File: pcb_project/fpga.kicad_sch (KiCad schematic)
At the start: 33 parts, among them U1 XC7A100T-FTG256

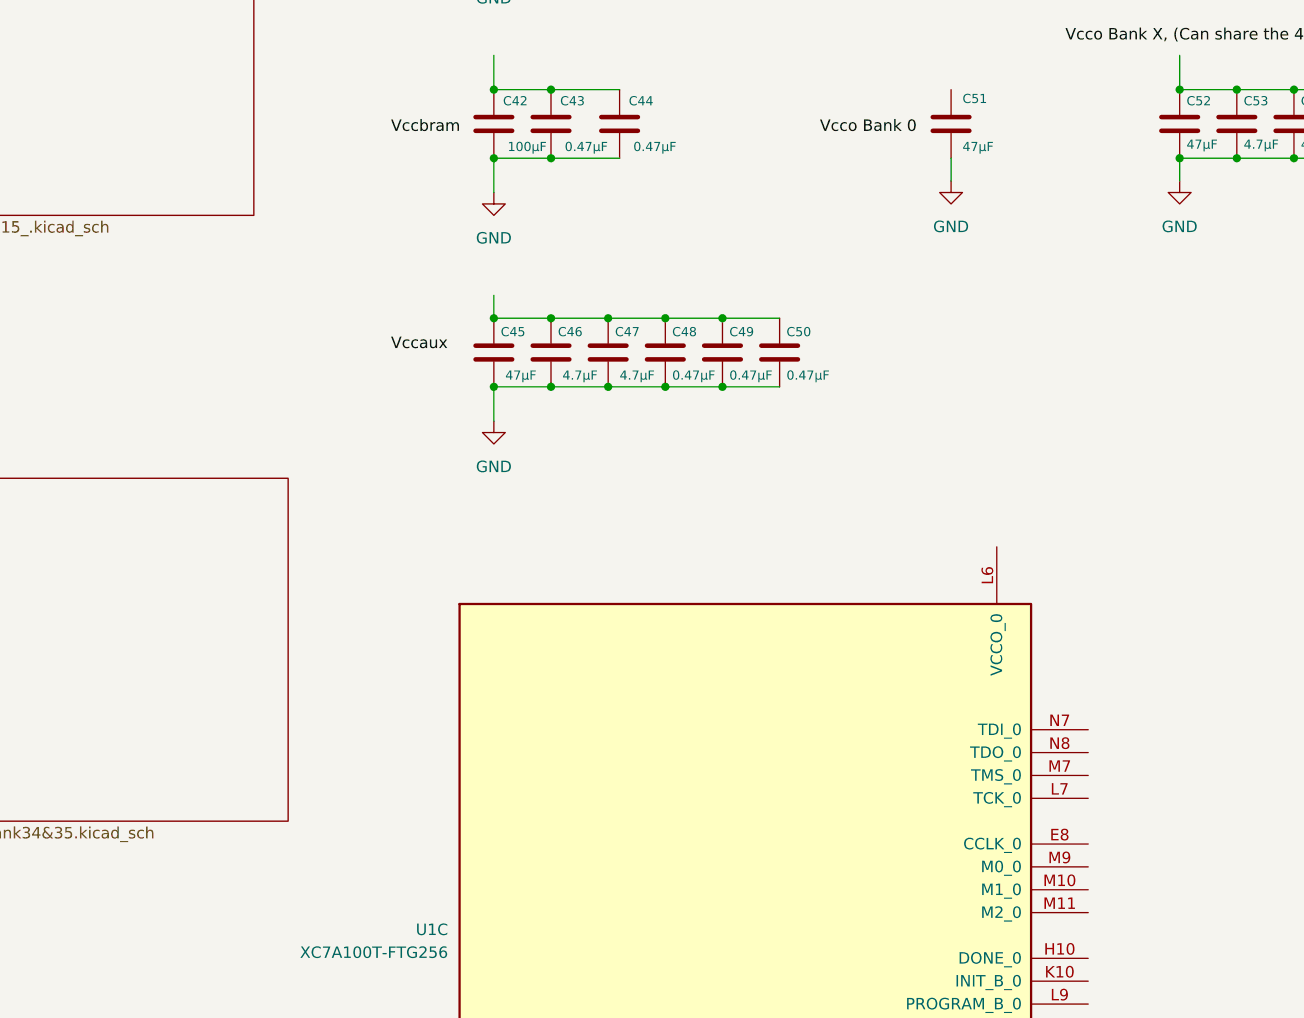
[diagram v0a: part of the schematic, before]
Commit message: Crystal + SPI flash FPGA
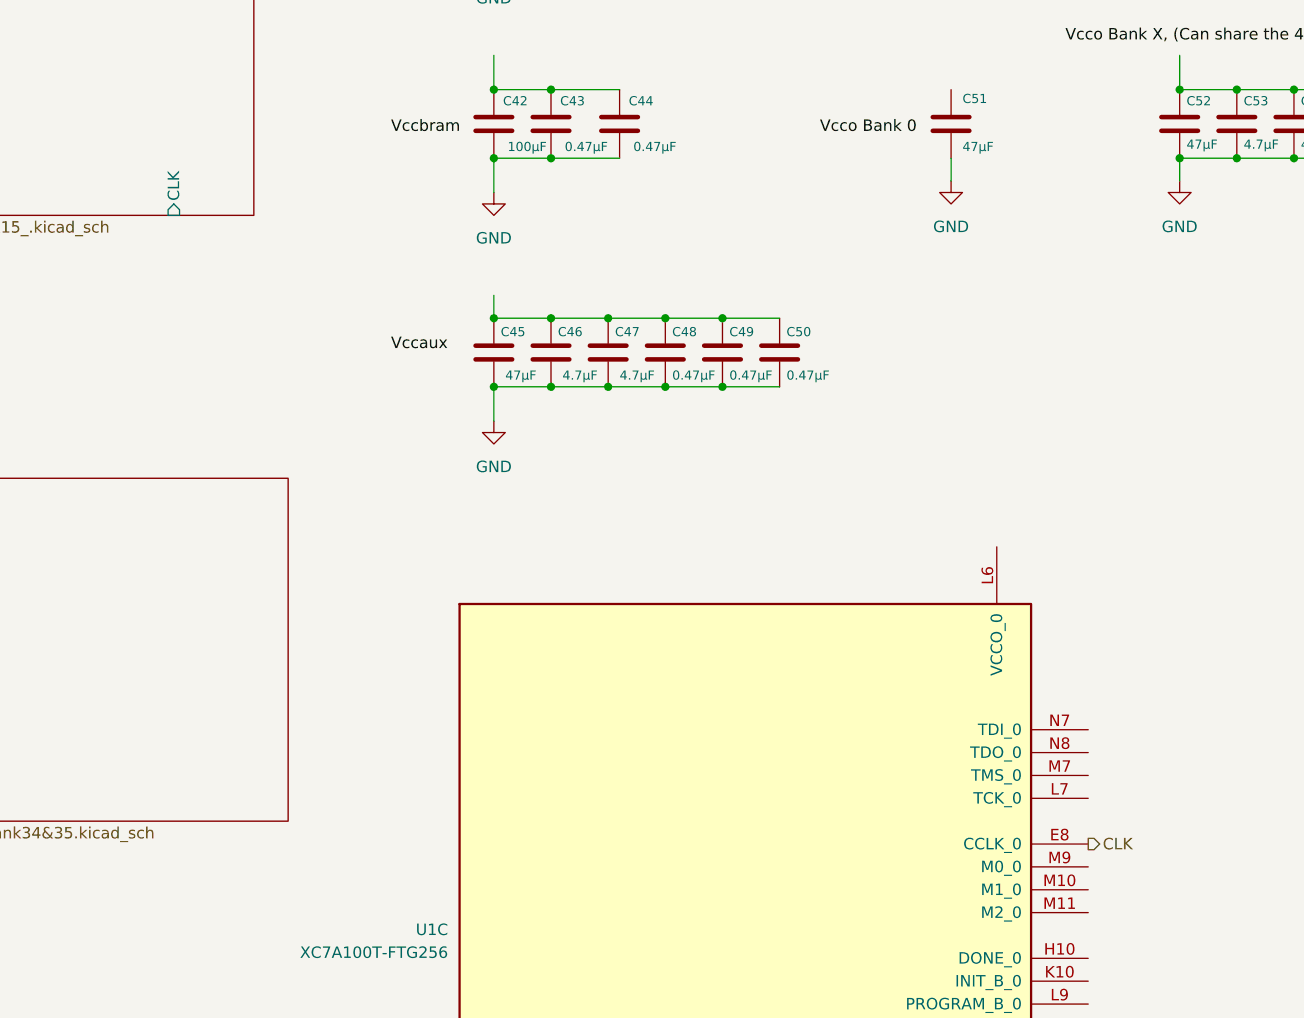
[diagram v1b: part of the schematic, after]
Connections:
- net CLK: now reaches U1.E8 (CCLK_0)
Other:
- sheet A_Bank14&15 ports: added CLK; removed none
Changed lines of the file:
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@@
 		)
 	)
+	(hierarchical_label "CLK"
+		(shape output)
+		(at 167.64 134.62 0)
+		(effects
+			(font
+				(size 1.27 1.27)
+			)
+			(justify left)
+		)
+	)
 	(symbol
 		(lib_id "Device:C")
@@
 			)
 		)
+		(pin "CLK" input
+			(at 66.04 64.77 270)
+			(effects
+				(font
+					(size 1.27 1.27)
+				)
+				(justify left)
+			)
+		)

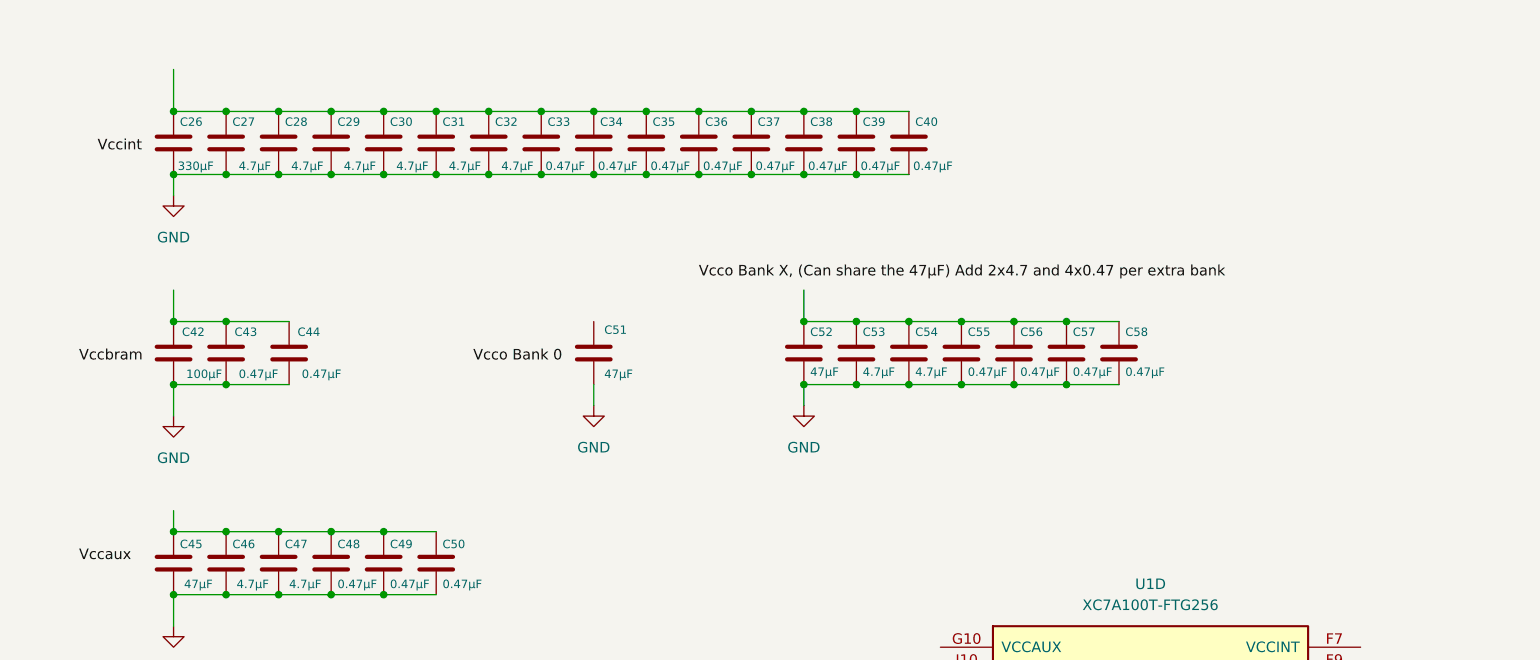
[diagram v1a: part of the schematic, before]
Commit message: Add framebuffer SRAM
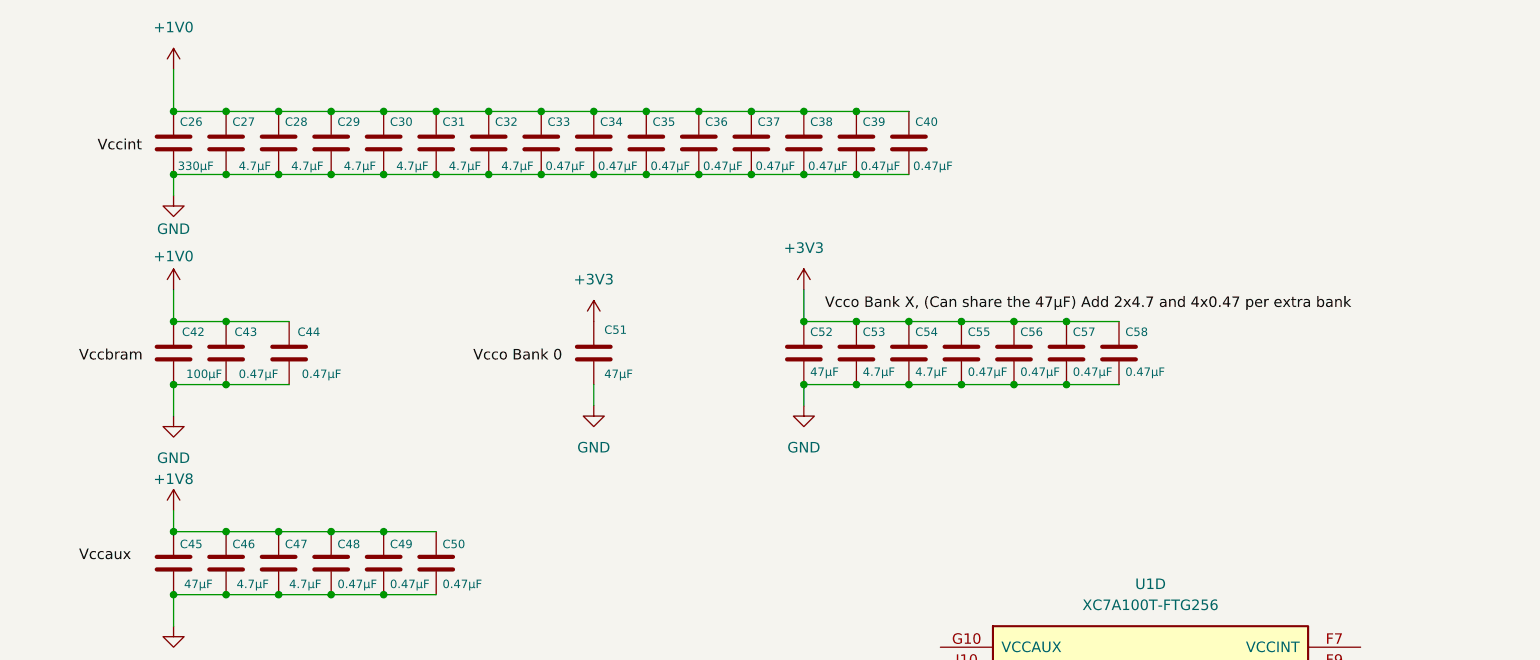
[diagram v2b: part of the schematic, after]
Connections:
- net +1V8: now reaches C45.1, C46.1, C47.1, C48.1, C49.1, C50.1
- net +3V3: now reaches C52.1, C53.1, C54.1, C55.1, C56.1, C57.1, C58.1
- net +3V3: now also C51.1
- net +1V0: now reaches C26.1, C27.1, C28.1, C29.1, C30.1, C31.1, C32.1, C33.1, C34.1, C35.1, C36.1, C37.1, C38.1, C39.1, C40.1
- net +1V0: now also C42.1, C43.1, C44.1

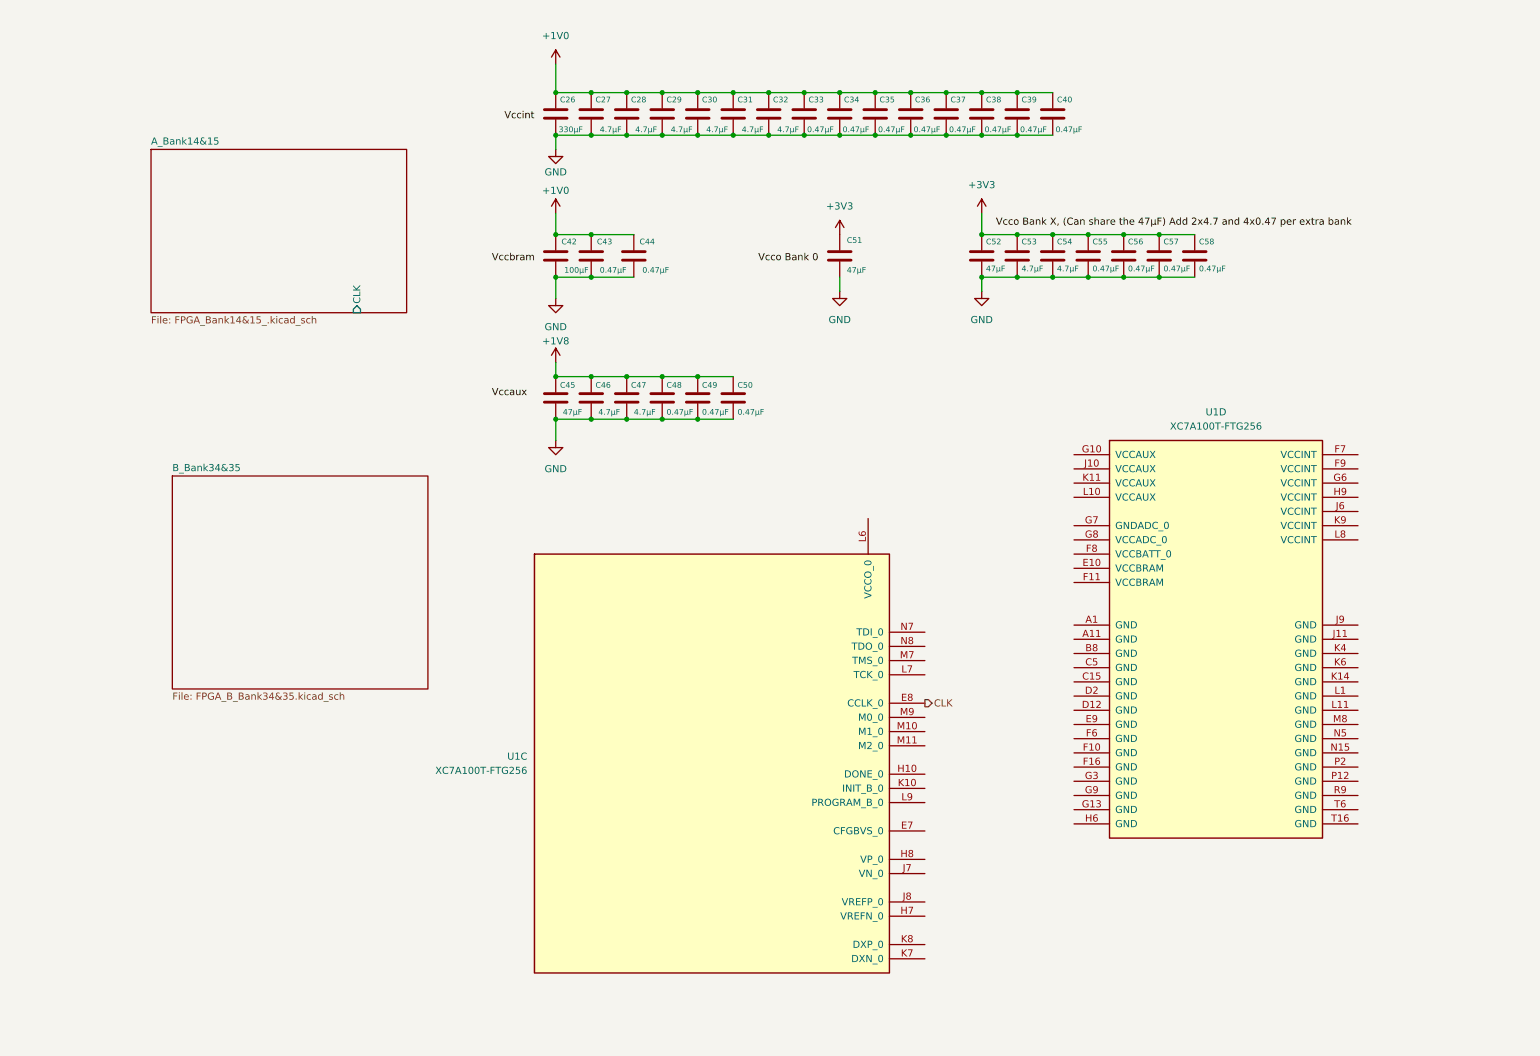
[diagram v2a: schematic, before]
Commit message: Add FPGA JTAG
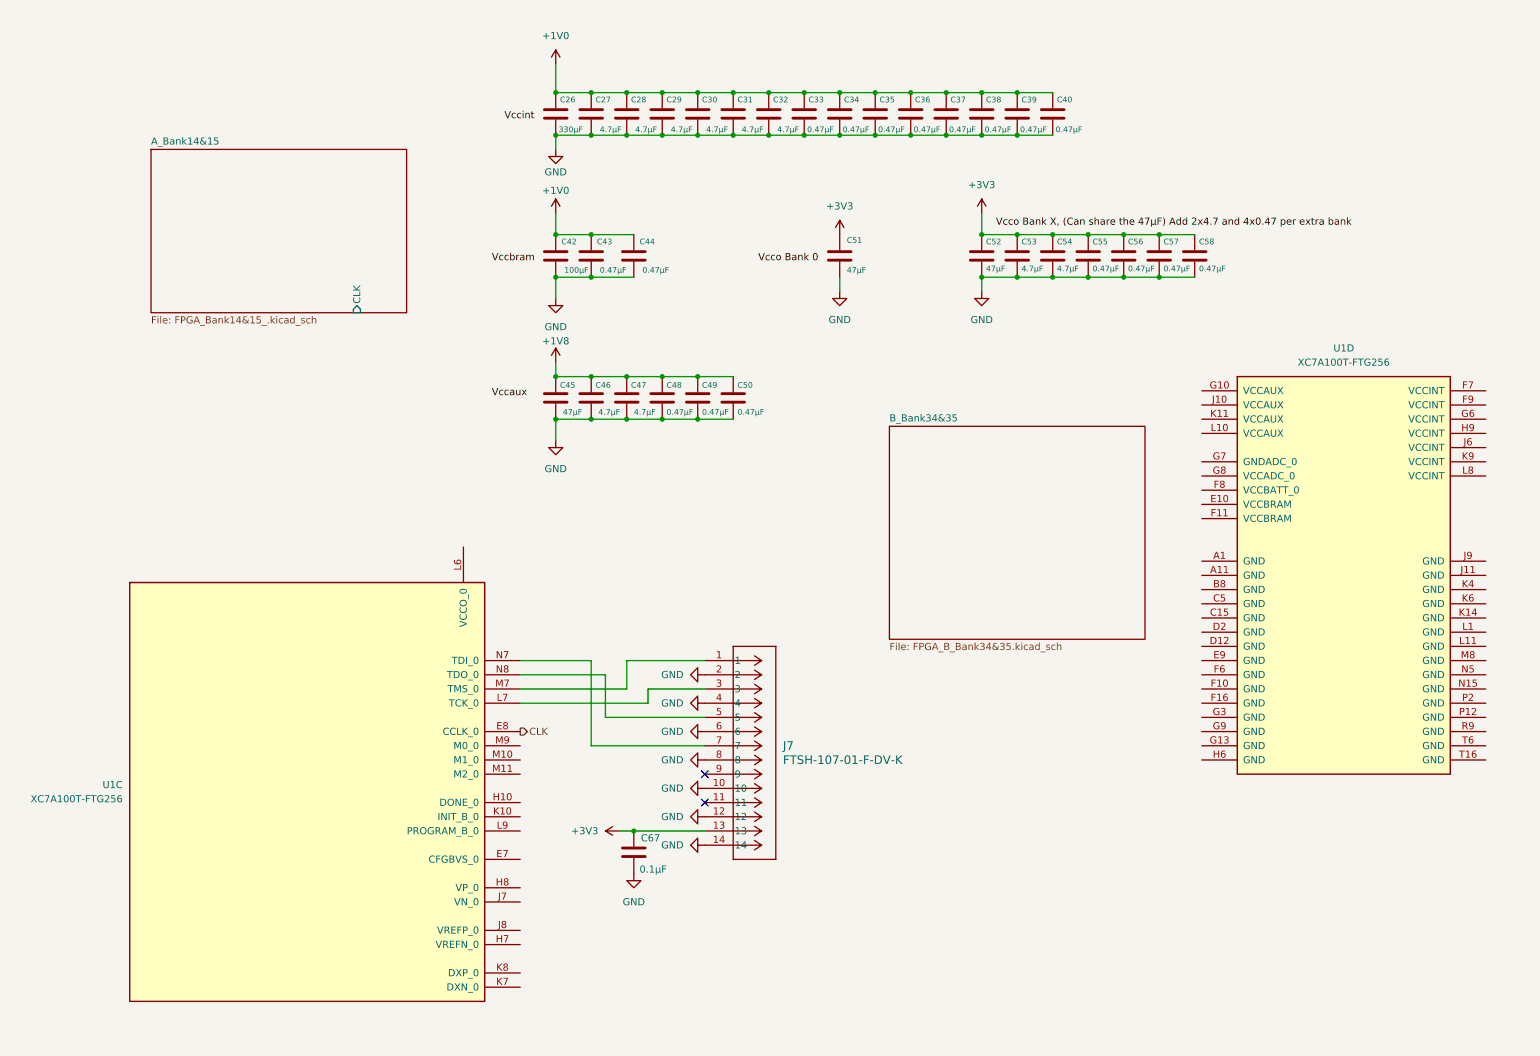
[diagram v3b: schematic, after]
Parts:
- added C67: 0.1µF, symbol Device:C
- added J7: FTSH-107-01-F-DV-K, CON14_2X7_DUK_FTSH_SAI, symbol 2025-09-21_16-27-56:FTSH-107-01-F-DV-K
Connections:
- net +3V3: now also C67.1, J7.13
- net GND: now also C67.2, J7.10, J7.12, J7.14, J7.2, J7.4, J7.6, J7.8
- net at U1.L7 (TCK_0): now also J7.3
- net at U1.M7 (TMS_0): now also J7.1
- net at U1.N7 (TDI_0): now also J7.7
- net at U1.N8 (TDO_0): now also J7.5
- no-connect marks 0 -> 2
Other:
- moved on the sheet: U1C, U1D

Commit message: 16bit binary weighted dac, FPGA power
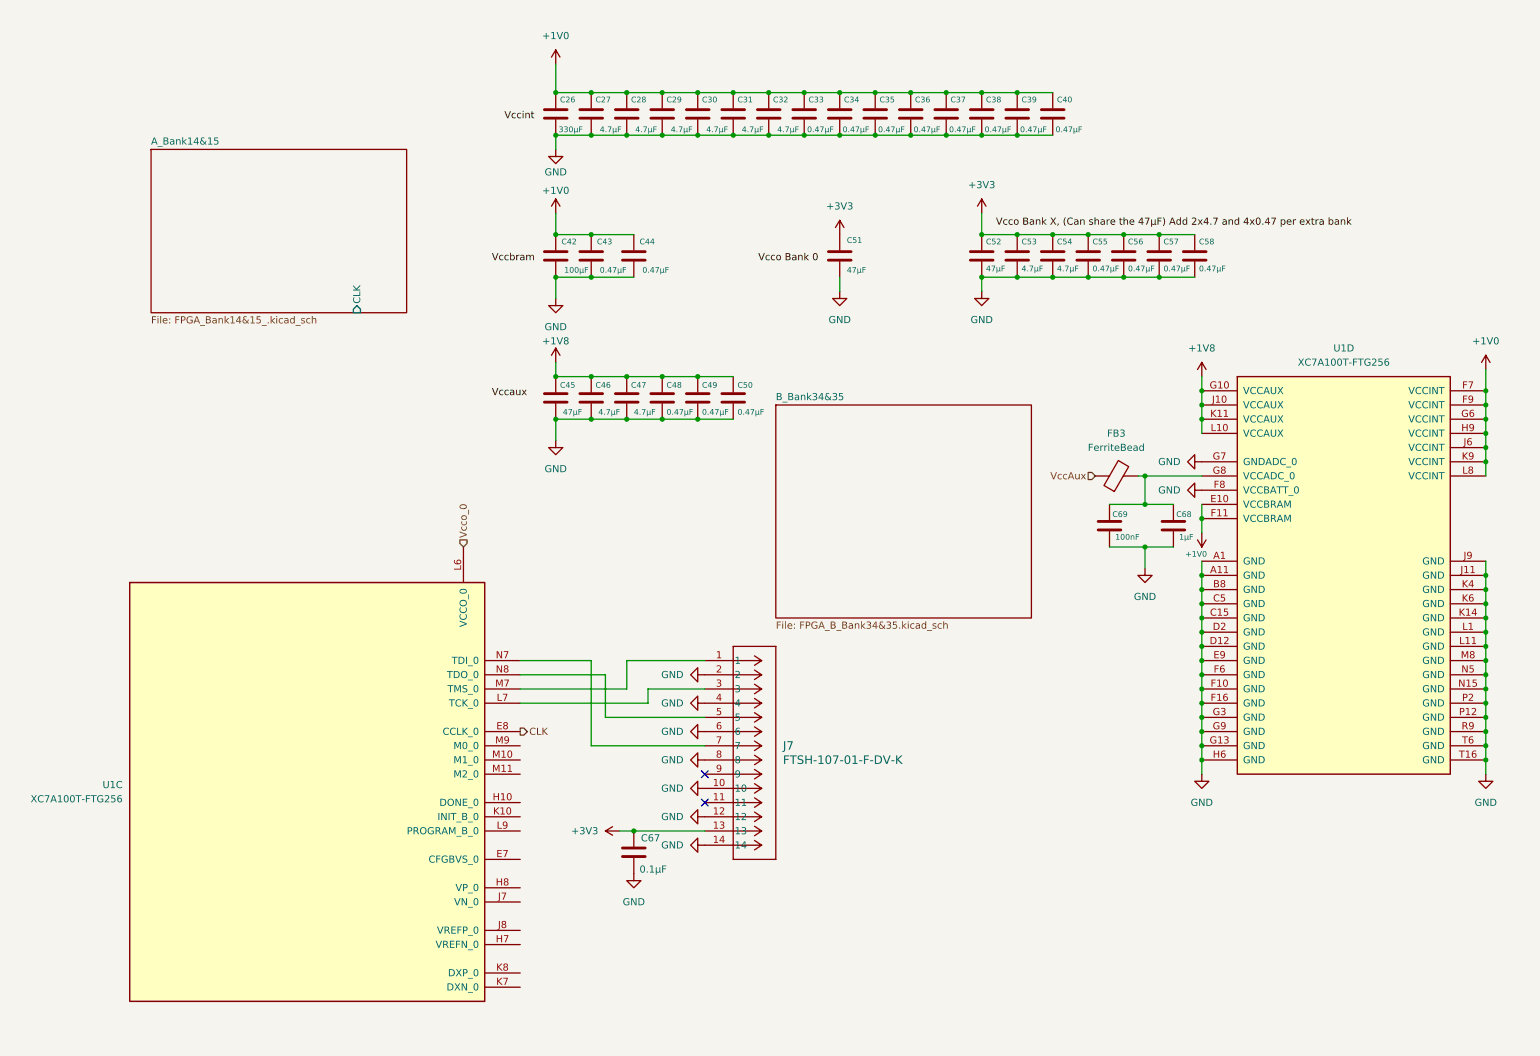
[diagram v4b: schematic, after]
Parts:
- added C68: 1µF, symbol Device:C
- added C69: 100nF, symbol Device:C
- added FB3: FerriteBead, symbol Device:FerriteBead
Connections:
- net +1V0: now also U1.E10 (VCCBRAM), U1.F11 (VCCBRAM), U1.F7 (VCCINT), U1.F9 (VCCINT), U1.G6 (VCCINT), U1.H9 (VCCINT), U1.J6 (VCCINT), U1.K9 (VCCINT), U1.L8 (VCCINT)
- net +1V8: now also U1.G10 (VCCAUX), U1.J10 (VCCAUX), U1.K11 (VCCAUX), U1.L10 (VCCAUX)
- net GND: now also U1.A1 (GND), U1.A11 (GND), U1.B8 (GND), U1.C15 (GND), U1.C5 (GND), U1.D12 (GND), U1.D2 (GND), U1.E9 (GND), U1.F10 (GND), U1.F16 (GND), U1.F6 (GND), U1.F8 (VCCBATT_0), U1.G13 (GND), U1.G3 (GND), U1.G7 (GNDADC_0), U1.G9 (GND), U1.H6 (GND), U1.J11 (GND), U1.J9 (GND), U1.K14 (GND), U1.K4 (GND), U1.K6 (GND), U1.L1 (GND), U1.L11 (GND), U1.M8 (GND), U1.N15 (GND), U1.N5 (GND), U1.P12 (GND), U1.P2 (GND), U1.R9 (GND), U1.T16 (GND), U1.T6 (GND), C68.2, C69.2
- net at U1.G8 (VCCADC_0): now also C68.1, C69.1, FB3.2
- net Vcco_0: now reaches U1.L6 (VCCO_0)
- new net VccAux: FB3.1
